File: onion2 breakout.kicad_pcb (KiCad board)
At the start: 2 copper layers, 40.6 x 55.9 mm, 14 parts, among them P1 USB_B, P2 USB_B, P3 CONN_01X16, P4 CONN_01X16, P5 CONN_01X16, P6 CONN_01X16, U1 CH340G, U2 AP1117, Y1 Crystal

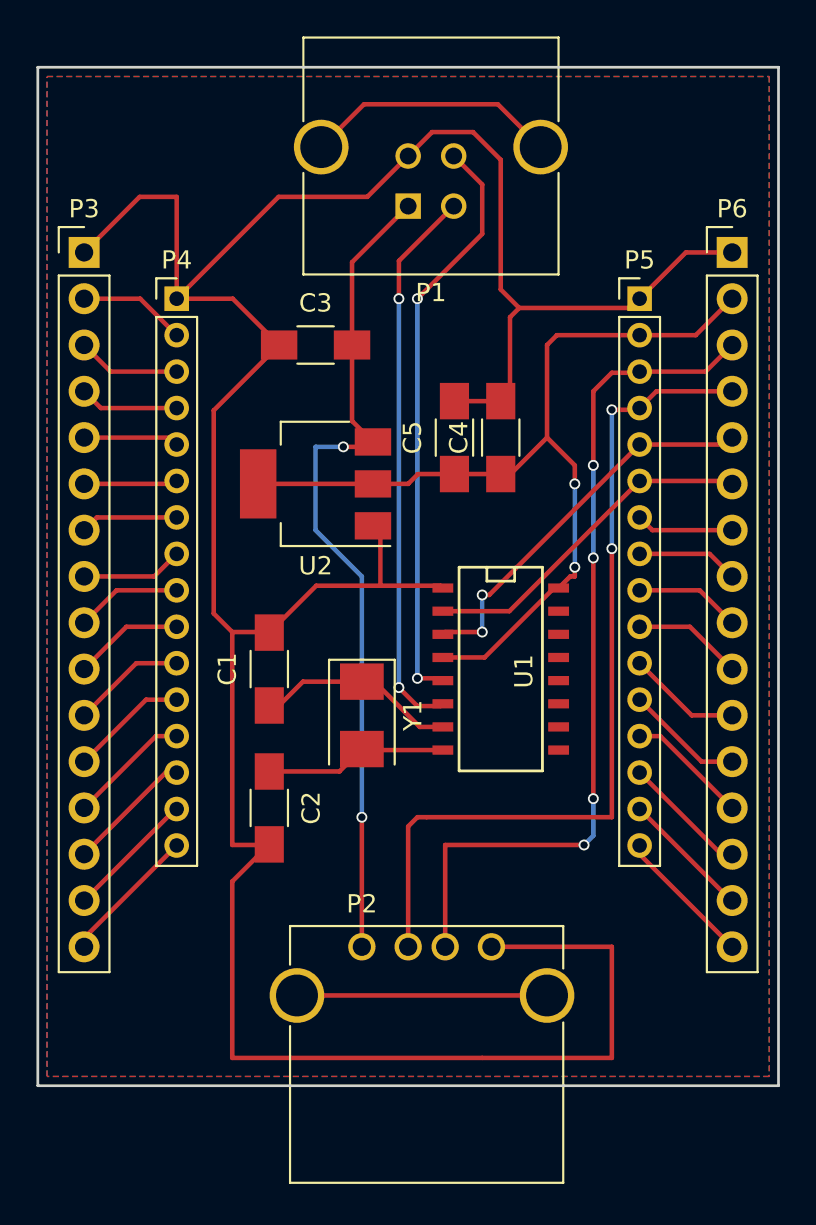
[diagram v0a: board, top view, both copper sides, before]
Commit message: Fxed Rx/Tx lines from CH340G to Onion. Adjusted header spacing to accomidate onion. Changed power/data connector from USB B to USB micro. Added BOM.
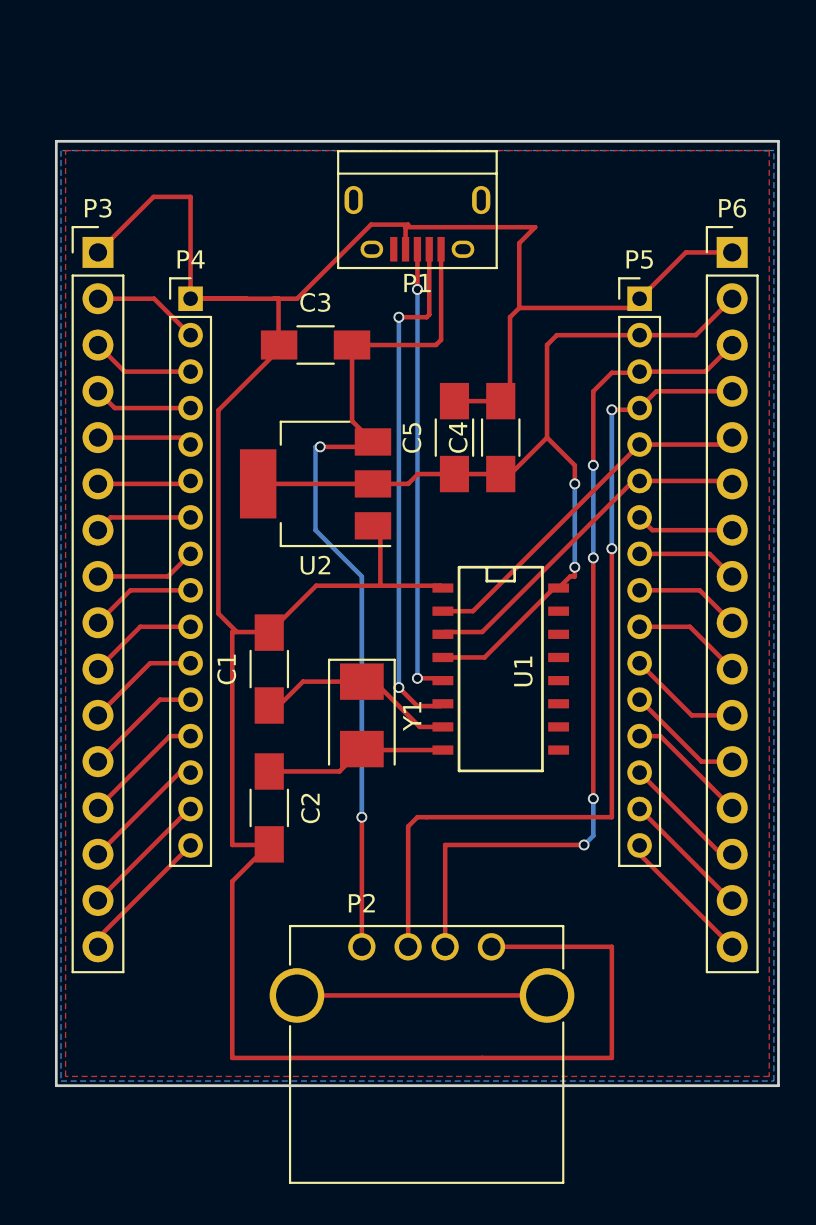
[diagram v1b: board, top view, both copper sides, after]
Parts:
- C1, C2: value C -> 22pF
- C3: value C -> 100uF
- C4: value C -> 10uF
- C5: value C -> 0.1uF
- P1: footprint Connect:USB_B_MUSB_Straight -> Connect:USB_Micro-B
- Y1: value Crystal -> 12MHz
- moved P1 1.14 mm to (99.6, 117.9)
- moved P3 0.76 mm to (82.0, 119.4)
- moved P4 0.76 mm to (87.1, 121.9)
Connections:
- U1 pad 2: TxD -> RxD
- U1 pad 3: RxD -> TxD
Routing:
- net Net-(P1-Pad5): track 14.0 -> 0.00 mm
- net D+: track 32.2 -> 25.0 mm
- net GND: track 164.0 -> 159.4 mm
- net D-: track 30.5 -> 28.5 mm
- net RxD: track 21.9 -> 20.2 mm, vias 2 -> 0
- net +5V: track 46.4 -> 47.5 mm
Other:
- board size 40.6 x 55.9 mm -> 39.6 x 51.8 mm
- rule trace_min: 0.2 -> 0.1524
- rule via_min_size: 0.4 -> 0.3302
- board text added: "Omega 2 Breakout - Rev 1"

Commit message: Corrected issue with u-USB pinout. Moved USB A connector down a bit for more clearance. Rev 2.0
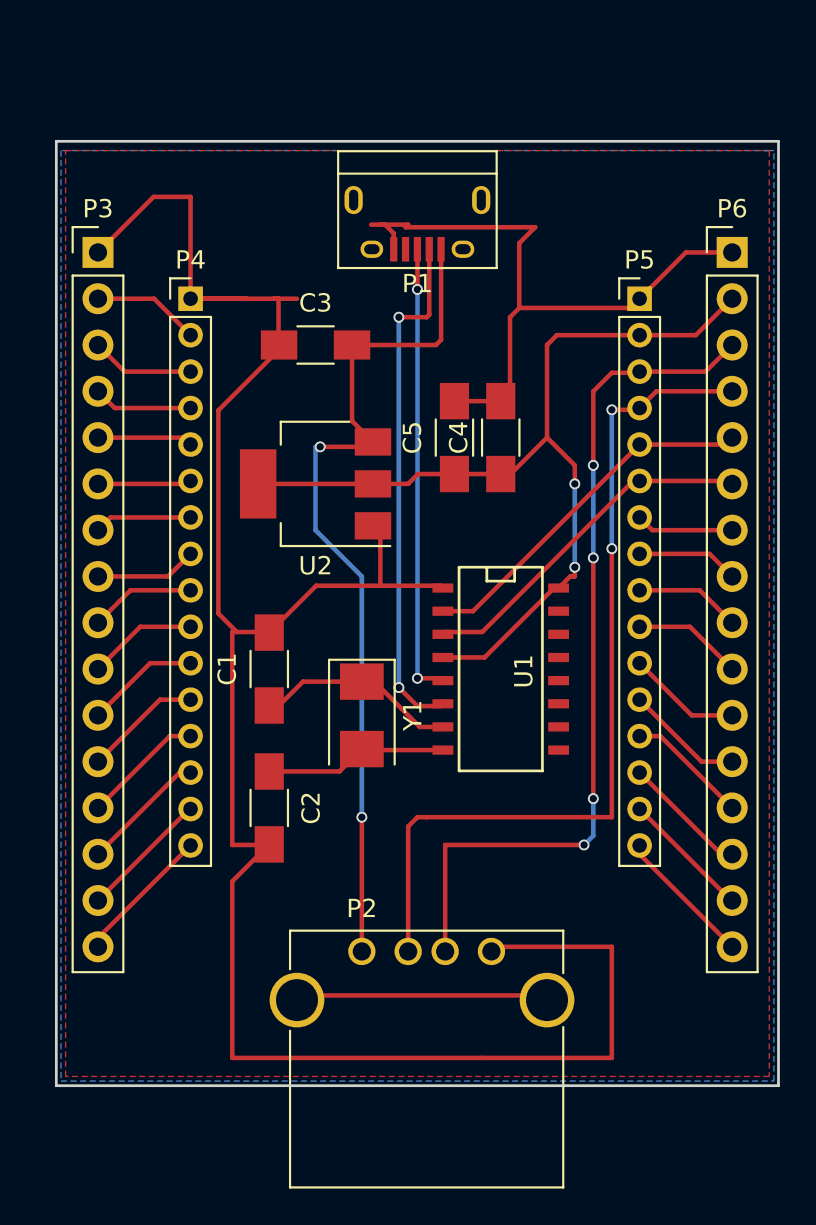
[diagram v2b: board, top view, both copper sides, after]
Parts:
- moved P2 0.25 mm to (96.5, 157.7)
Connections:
- P1 pad 4: GND -> Net-(P1-Pad4)
- P1 pad 5: Net-(P1-Pad5) -> GND
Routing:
- net GND: track 159.4 -> 154.2 mm
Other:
- board text added: "Omega 2 Breakout - Rev 2"
- board text removed: "Omega 2 Breakout - Rev 1"

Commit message: Updated footprint of microUSB connector to avoid slitted hole.
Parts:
- P1: footprint Connect:USB_Micro-B -> USB-micro -oshpark:USB_Micro-B
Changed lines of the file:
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@@
     (links 62)
     (no_connects 0)
-    (area 79.680999 113.208999 119.455001 165.175001)
+    (area 76.933667 111.721 121.948334 171.159001)
     (thickness 1.6)
     (drawings 5)
@@
   (page A4)
   (layers
-    (0 F.Cu signal)
-    (31 B.Cu signal)
+    (0 F.Cu signal hide)
+    (31 B.Cu signal hide)
     (32 B.Adhes user hide)
     (33 F.Adhes user hide)
@@
     )
   )
-  (module Connect:USB_Micro-B (layer F.Cu)
+  (module "USB-micro -oshpark:USB_Micro-B" (layer F.Cu)
     (at 99.568 117.856 180)
     (descr "Micro USB Type B Receptacle")
@@
     (pad 5 smd rect (at 1.3 -1.35 270) (size 1.35 0.4) (layers F.Cu F.Paste F.Mask)
       (net 2 GND))
-    (pad 6 thru_hole oval (at -2.5 -1.35 270) (size 0.95 1.25) (drill oval 0.55 0.85) (layers *.Cu *.Mask))
-    (pad 6 thru_hole oval (at 2.5 -1.35 270) (size 0.95 1.25) (drill oval 0.55 0.85) (layers *.Cu *.Mask))
-    (pad 6 thru_hole oval (at -3.5 1.35 270) (size 1.55 1) (drill oval 1.15 0.5) (layers *.Cu *.Mask))
-    (pad 6 thru_hole oval (at 3.5 1.35 270) (size 1.55 1) (drill oval 1.15 0.5) (layers *.Cu *.Mask))
+    (pad 6 thru_hole oval (at -2.5 -1.35 270) (size 0.95 1.15) (drill 0.75) (layers *.Cu *.Mask))
+    (pad 6 thru_hole oval (at 2.5 -1.35 270) (size 0.95 1.15) (drill 0.75) (layers *.Cu *.Mask))
+    (pad 6 thru_hole oval (at -3.5 1.35 270) (size 1.55 1.25) (drill 1.2) (layers *.Cu *.Mask))
+    (pad 6 thru_hole oval (at 3.5 1.35 270) (size 1.55 1.25) (drill 1.2) (layers *.Cu *.Mask))
   )
   (gr_text "Omega 2 Breakout - Rev 2" (at 100.076 163.322) (layer B.SilkS)
